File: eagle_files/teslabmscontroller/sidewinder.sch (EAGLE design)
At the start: 42 parts, among them J1 TERMINAL12, J2 TERMINAL12, Q1 2N3704, Q2 2N3906, T1 V_REG_317SINK, U1 G3VM41, U2 G3VM41, U3 G3VM41, U4 SN65HVD230, U5 SP720APP, U6 SP720APP

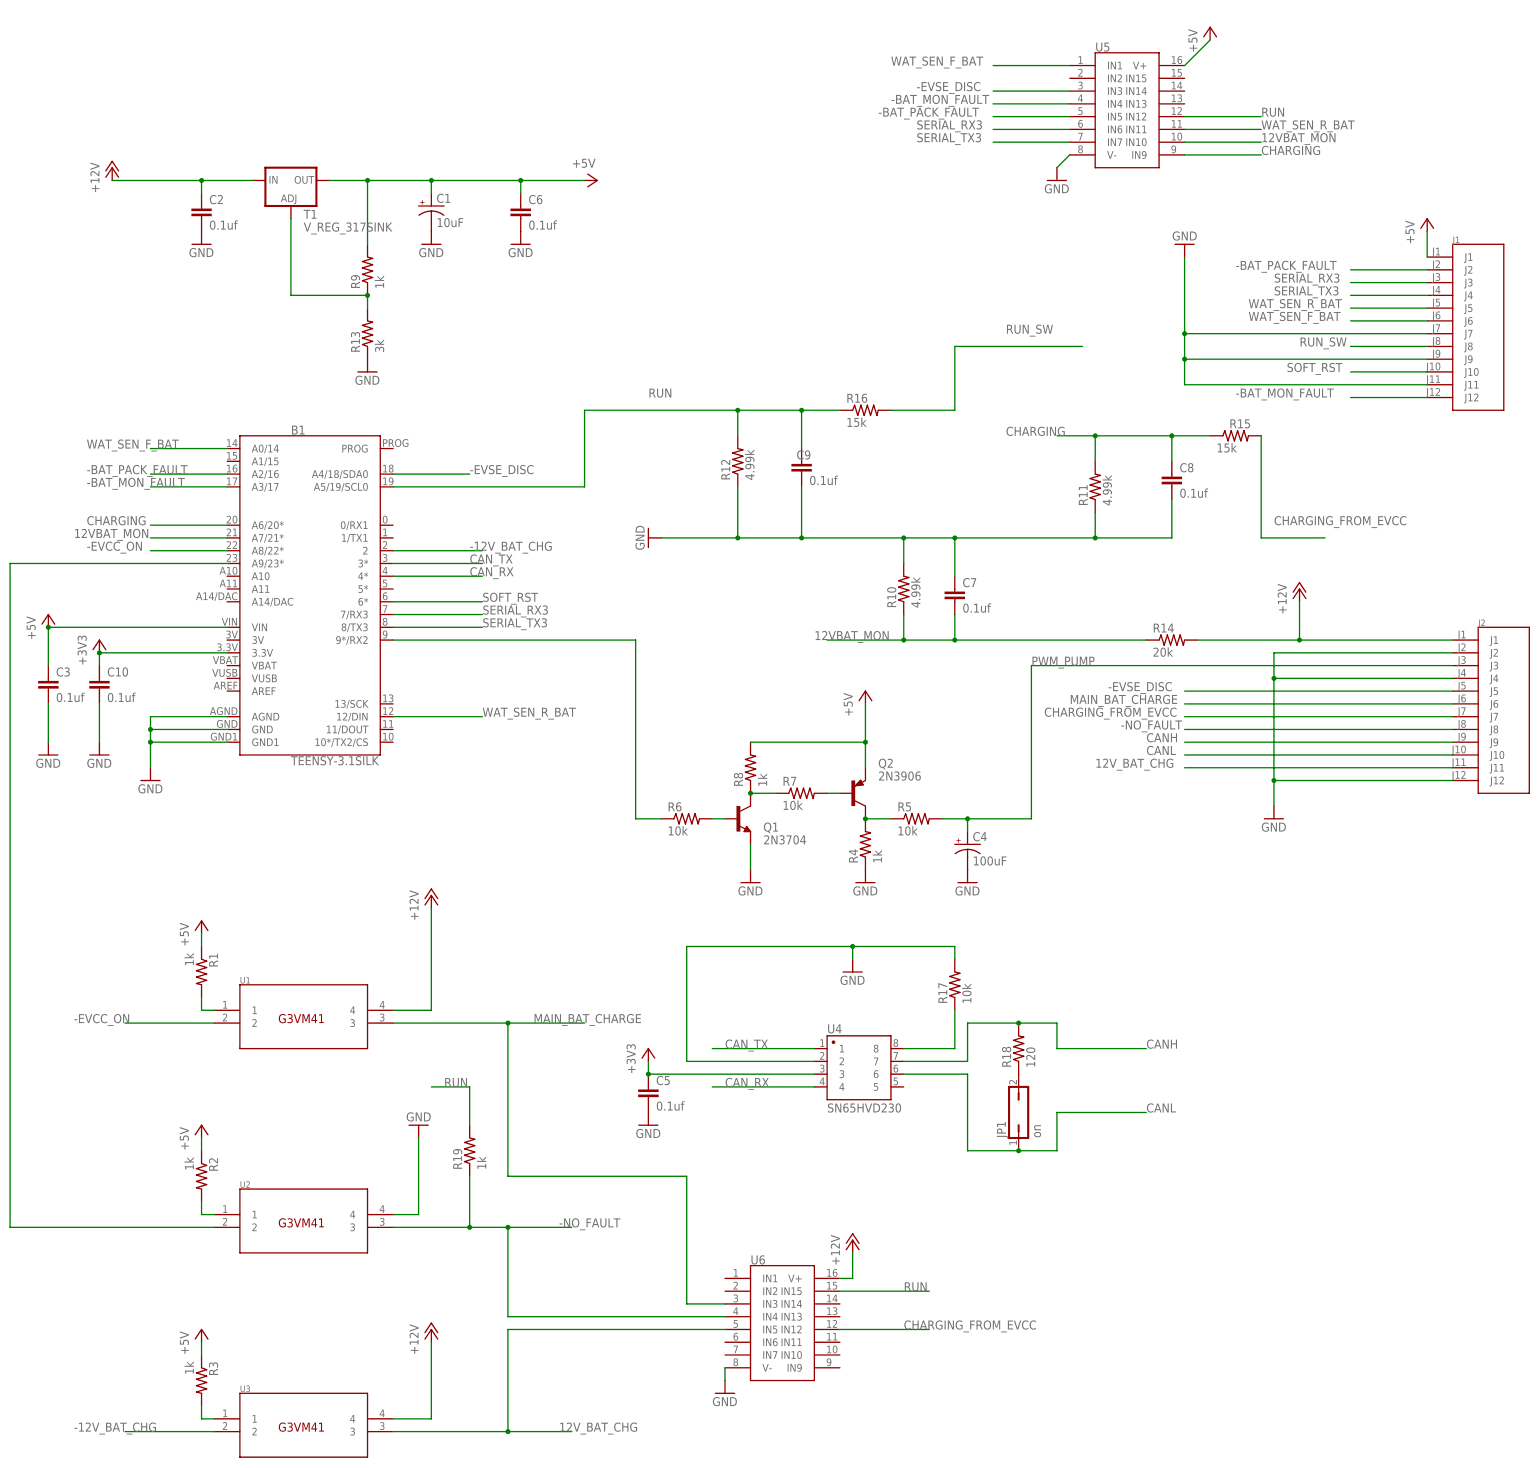
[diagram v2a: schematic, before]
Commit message: added EVCC_config.txt
added the config of the EVCC controller
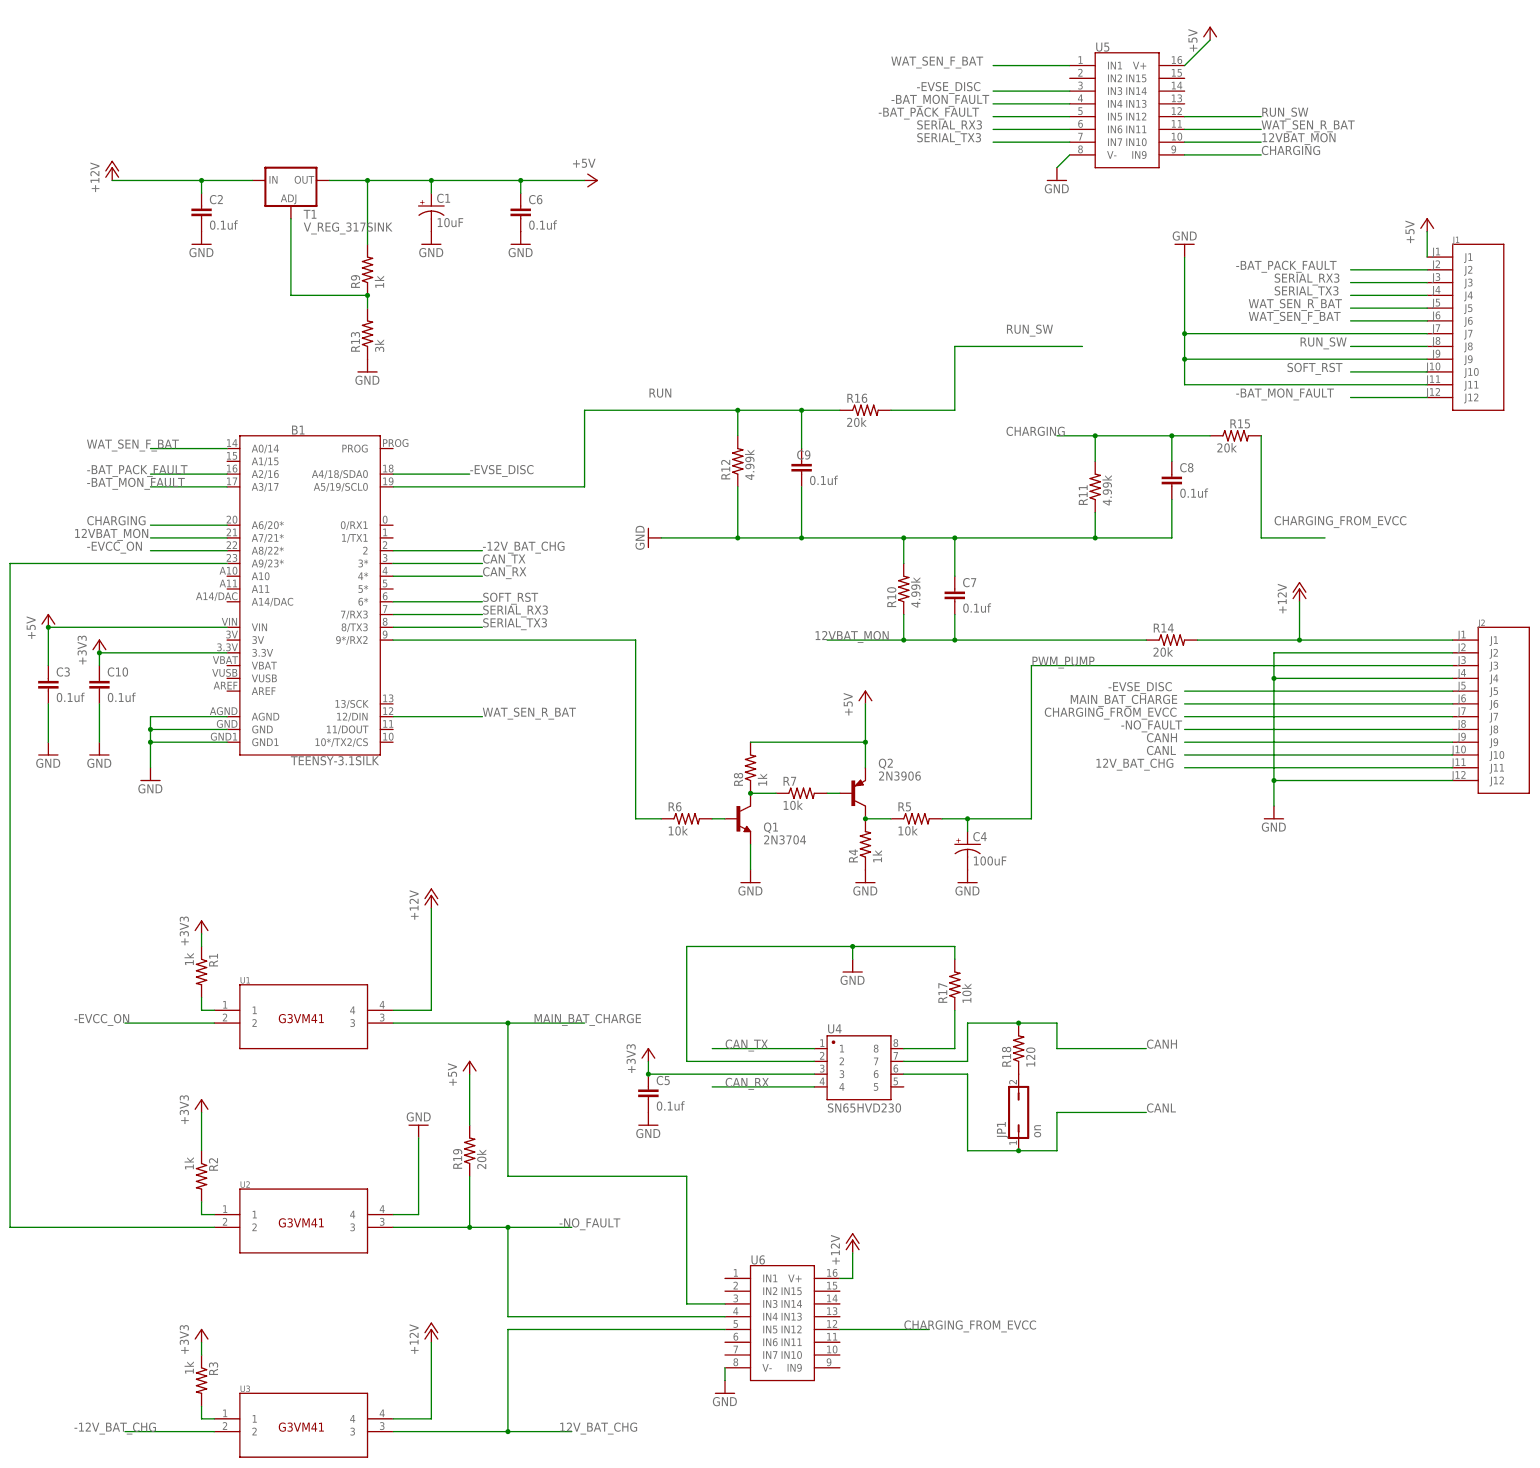
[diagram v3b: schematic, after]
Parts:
- R15, R16: value 15k -> 20k
- R19: value 1k -> 20k
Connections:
- net +3V3: now also R1.1, R2.1, R3.1
- net +5V: now also R19.2; no longer R1.1, R2.1, R3.1
- net RUN: no longer R19.2, U5.IN12, U6.IN15
- net RUN_SW: now also U5.IN12
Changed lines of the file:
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@@
 <part name="GND3" library="supply1" library_urn="urn:adsk.eagle:library:371" deviceset="GND" device=""/>
 <part name="R12" library="rcl" library_urn="urn:adsk.eagle:library:334" deviceset="R-US_" device="0207/10" package3d_urn="urn:adsk.eagle:package:23491/2" value="4.99k"/>
-<part name="R16" library="rcl" library_urn="urn:adsk.eagle:library:334" deviceset="R-US_" device="0207/10" package3d_urn="urn:adsk.eagle:package:23491/2" value="15k"/>
+<part name="R16" library="rcl" library_urn="urn:adsk.eagle:library:334" deviceset="R-US_" device="0207/10" package3d_urn="urn:adsk.eagle:package:23491/2" value="20k"/>
 <part name="GND4" library="supply1" library_urn="urn:adsk.eagle:library:371" deviceset="GND" device=""/>
-<part name="R15" library="rcl" library_urn="urn:adsk.eagle:library:334" deviceset="R-US_" device="0207/10" package3d_urn="urn:adsk.eagle:package:23491/2" value="15k"/>
+<part name="R15" library="rcl" library_urn="urn:adsk.eagle:library:334" deviceset="R-US_" device="0207/10" package3d_urn="urn:adsk.eagle:package:23491/2" value="20k"/>
 <part name="R11" library="rcl" library_urn="urn:adsk.eagle:library:334" deviceset="R-US_" device="0207/10" package3d_urn="urn:adsk.eagle:package:23491/2" value="4.99k"/>
 <part name="R14" library="rcl" library_urn="urn:adsk.eagle:library:334" deviceset="R-US_" device="0207/10" package3d_urn="urn:adsk.eagle:package:23491/2" value="20k"/>
@@
 <part name="GND5" library="supply1" library_urn="urn:adsk.eagle:library:371" deviceset="GND" device=""/>
 <part name="R1" library="rcl" library_urn="urn:adsk.eagle:library:334" deviceset="R-US_" device="0207/10" package3d_urn="urn:adsk.eagle:package:23491/2" value="1k"/>
-<part name="P+4" library="supply1" library_urn="urn:adsk.eagle:library:371" deviceset="+5V" device=""/>
 <part name="P+5" library="supply1" library_urn="urn:adsk.eagle:library:371" deviceset="+12V" device=""/>
 <part name="P+6" library="supply1" library_urn="urn:adsk.eagle:library:371" deviceset="+12V" device=""/>
-<part name="P+7" library="supply1" library_urn="urn:adsk.eagle:library:371" deviceset="+5V" device=""/>
 <part name="R2" library="rcl" library_urn="urn:adsk.eagle:library:334" deviceset="R-US_" device="0207/10" package3d_urn="urn:adsk.eagle:package:23491/2" value="1k"/>
 <part name="R3" library="rcl" library_urn="urn:adsk.eagle:library:334" deviceset="R-US_" device="0207/10" package3d_urn="urn:adsk.eagle:package:23491/2" value="1k"/>
-<part name="P+8" library="supply1" library_urn="urn:adsk.eagle:library:371" deviceset="+5V" device=""/>
 <part name="P+9" library="supply1" library_urn="urn:adsk.eagle:library:371" deviceset="+12V" device=""/>
 <part name="GND9" library="supply1" library_urn="urn:adsk.eagle:library:371" deviceset="GND" device=""/>
@@
 <part name="C1" library="SparkFun-Capacitors" library_urn="urn:adsk.eagle:library:510" deviceset="10UF-POLAR" device="-RADIAL-2.5MM-25V-20%" package3d_urn="urn:adsk.eagle:package:37423/1" value="10uF"/>
 <part name="U4" library="SparkFun-Retired" deviceset="GENERIC-SOIC8" device="MSGEQ7N-FILTER" value="SN65HVD230"/>
-<part name="R19" library="rcl" library_urn="urn:adsk.eagle:library:334" deviceset="R-US_" device="0207/10" package3d_urn="urn:adsk.eagle:package:23491/2" value="1k"/>
+<part name="R19" library="rcl" library_urn="urn:adsk.eagle:library:334" deviceset="R-US_" device="0207/10" package3d_urn="urn:adsk.eagle:package:23491/2" value="20k"/>
+<part name="+3V3" library="supply1" library_urn="urn:adsk.eagle:library:371" deviceset="+3V3" device=""/>
+<part name="+3V4" library="supply1" library_urn="urn:adsk.eagle:library:371" deviceset="+3V3" device=""/>
+<part name="+3V5" library="supply1" library_urn="urn:adsk.eagle:library:371" deviceset="+3V3" device=""/>
+<part name="P+4" library="supply1" library_urn="urn:adsk.eagle:library:371" deviceset="+5V" device=""/>
 </parts>
 <sheets>
@@
 <attribute name="VALUE" x="9.398" y="-11.43" size="1.778" layer="96" rot="R270"/>
 </instance>
-<instance part="P+4" gate="1" x="12.7" y="-5.08" smashed="yes">
-<attribute name="VALUE" x="10.16" y="-10.16" size="1.778" layer="96" rot="R90"/>
-</instance>
 <instance part="P+5" gate="1" x="231.14" y="60.96" smashed="yes">
 <attribute name="VALUE" x="228.6" y="55.88" size="1.778" layer="96" rot="R90"/>
@@
 <instance part="P+6" gate="1" x="58.42" y="0" smashed="yes">
 <attribute name="VALUE" x="55.88" y="-5.08" size="1.778" layer="96" rot="R90"/>
-</instance>
-<instance part="P+7" gate="1" x="12.7" y="-45.72" smashed="yes">
-<attribute name="VALUE" x="10.16" y="-50.8" size="1.778" layer="96" rot="R90"/>
 </instance>
 <instance part="R2" gate="G$1" x="12.7" y="-55.88" smashed="yes" rot="R270">
@@
 <attribute name="VALUE" x="9.398" y="-92.71" size="1.778" layer="96" rot="R270"/>
 </instance>
-<instance part="P+8" gate="1" x="12.7" y="-86.36" smashed="yes">
-<attribute name="VALUE" x="10.16" y="-91.44" size="1.778" layer="96" rot="R90"/>
-</instance>
 <instance part="P+9" gate="1" x="58.42" y="-86.36" smashed="yes">
 <attribute name="VALUE" x="55.88" y="-91.44" size="1.778" layer="96" rot="R90"/>
@@
 <attribute name="NAME" x="64.5414" y="-54.61" size="1.778" layer="95" rot="R90"/>
 <attribute name="VALUE" x="69.342" y="-54.61" size="1.778" layer="96" rot="R90"/>
+</instance>
+<instance part="+3V3" gate="G$1" x="12.7" y="-40.64" smashed="yes">
+<attribute name="VALUE" x="10.16" y="-45.72" size="1.778" layer="96" rot="R90"/>
+</instance>
+<instance part="+3V4" gate="G$1" x="12.7" y="-5.08" smashed="yes">
+<attribute name="VALUE" x="10.16" y="-10.16" size="1.778" layer="96" rot="R90"/>
+</instance>
+<instance part="+3V5" gate="G$1" x="12.7" y="-86.36" smashed="yes">
+<attribute name="VALUE" x="10.16" y="-91.44" size="1.778" layer="96" rot="R90"/>
+</instance>
+<instance part="P+4" gate="1" x="66.04" y="-33.02" smashed="yes">
+<attribute name="VALUE" x="63.5" y="-38.1" size="1.778" layer="96" rot="R90"/>
 </instance>
 </instances>
@@
 <wire x1="256.54" y1="132.08" x2="256.54" y2="127" width="0.1524" layer="91"/>
 <pinref part="J1" gate="G$1" pin="J1"/>
-</segment>
-<segment>
-<pinref part="R1" gate="G$1" pin="1"/>
-<pinref part="P+4" gate="1" pin="+5V"/>
-<wire x1="12.7" y1="-10.16" x2="12.7" y2="-7.62" width="0.1524" layer="91"/>
-</segment>
-<segment>
-<pinref part="P+7" gate="1" pin="+5V"/>
-<pinref part="R2" gate="G$1" pin="1"/>
-<wire x1="12.7" y1="-48.26" x2="12.7" y2="-50.8" width="0.1524" layer="91"/>
-</segment>
-<segment>
-<pinref part="R3" gate="G$1" pin="1"/>
-<pinref part="P+8" gate="1" pin="+5V"/>
-<wire x1="12.7" y1="-91.44" x2="12.7" y2="-88.9" width="0.1524" layer="91"/>
 </segment>
 <segment>
@@
 <junction x="-17.78" y="53.34"/>
 <pinref part="C3" gate="G$1" pin="1"/>
+</segment>
+<segment>
+<pinref part="R19" gate="G$1" pin="2"/>
+<wire x1="66.04" y1="-45.72" x2="66.04" y2="-35.56" width="0.1524" layer="91"/>
+<pinref part="P+4" gate="1" pin="+5V"/>
 </segment>
 </net>
@@
 <pinref part="B1" gate="G$1" pin="2"/>
 <wire x1="50.8" y1="68.58" x2="68.58" y2="68.58" width="0.1524" layer="91"/>
-<label x="66.04" y="68.58" size="1.778" layer="95"/>
+<label x="68.58" y="68.58" size="1.778" layer="95"/>
 </segment>
 <segment>
@@
 <pinref part="C10" gate="G$1" pin="1"/>
 </segment>
+<segment>
+<pinref part="R1" gate="G$1" pin="1"/>
+<wire x1="12.7" y1="-10.16" x2="12.7" y2="-7.62" width="0.1524" layer="91"/>
+<pinref part="+3V4" gate="G$1" pin="+3V3"/>
+</segment>
+<segment>
+<pinref part="R2" gate="G$1" pin="1"/>
+<wire x1="12.7" y1="-43.18" x2="12.7" y2="-50.8" width="0.1524" layer="91"/>
+<pinref part="+3V3" gate="G$1" pin="+3V3"/>
+</segment>
+<segment>
+<pinref part="R3" gate="G$1" pin="1"/>
+<wire x1="12.7" y1="-91.44" x2="12.7" y2="-88.9" width="0.1524" layer="91"/>
+<pinref part="+3V5" gate="G$1" pin="+3V3"/>
+</segment>
 </net>
 <net name="CAN_TX" class="0">
@@
 <pinref part="B1" gate="G$1" pin="3*"/>
 <wire x1="50.8" y1="66.04" x2="68.58" y2="66.04" width="0.1524" layer="91"/>
-<label x="66.04" y="66.04" size="1.778" layer="95"/>
+<label x="68.58" y="66.04" size="1.778" layer="95"/>
 </segment>
 </net>
@@
 <pinref part="B1" gate="G$1" pin="4*"/>
 <wire x1="50.8" y1="63.5" x2="68.58" y2="63.5" width="0.1524" layer="91"/>
-<label x="66.04" y="63.5" size="1.778" layer="95"/>
+<label x="68.58" y="63.5" size="1.778" layer="95"/>
 </segment>
 </net>
@@
 </net>
 <net name="RUN" class="0">
-<segment>
-<pinref part="R19" gate="G$1" pin="2"/>
-<wire x1="66.04" y1="-45.72" x2="66.04" y2="-38.1" width="0.1524" layer="91"/>
-<wire x1="66.04" y1="-38.1" x2="58.42" y2="-38.1" width="0.1524" layer="91"/>
-<label x="60.96" y="-38.1" size="1.778" layer="95"/>
-</segment>
-<segment>
-<pinref part="U6" gate="G$1" pin="IN15"/>
-<wire x1="139.7" y1="-78.74" x2="157.48" y2="-78.74" width="0.1524" layer="91"/>
-<label x="152.4" y="-78.74" size="1.778" layer="95"/>
-</segment>
-<segment>
-<pinref part="U5" gate="G$1" pin="IN12"/>
-<wire x1="208.28" y1="154.94" x2="223.52" y2="154.94" width="0.1524" layer="91"/>
-<label x="223.52" y="154.94" size="1.778" layer="95"/>
-</segment>
 <segment>
 <pinref part="R16" gate="G$1" pin="1"/>
@@
 <label x="231.14" y="109.22" size="1.778" layer="95"/>
 </segment>
-</net>
+<segment>
+<pinref part="U5" gate="G$1" pin="IN12"/>
+<wire x1="208.28" y1="154.94" x2="223.52" y2="154.94" width="0.1524" layer="91"/>
+<label x="223.52" y="154.94" size="1.778" layer="95"/>
+</segment>
+</net>
